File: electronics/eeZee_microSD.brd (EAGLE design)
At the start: 19.8 x 18.3 mm, 13 parts, among them U1 MIC5317, U2 74HC4050, U4 MICROSD_CD

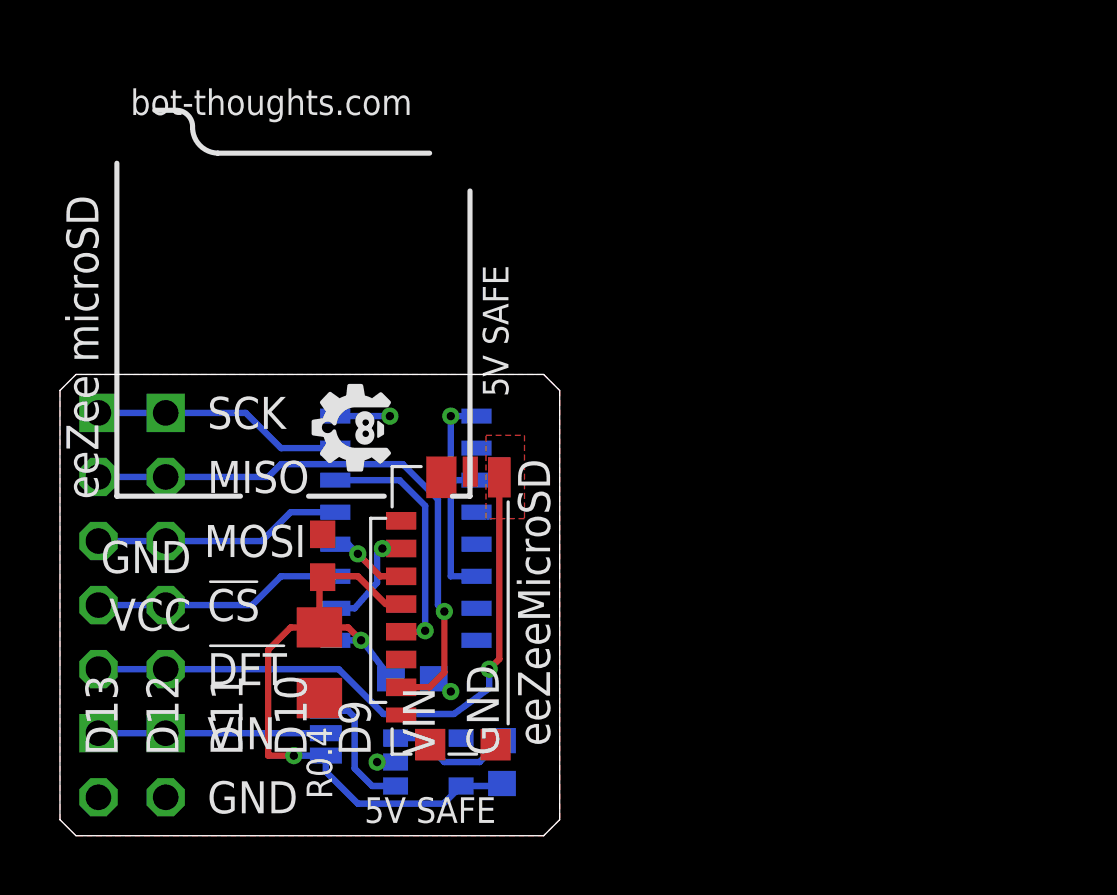
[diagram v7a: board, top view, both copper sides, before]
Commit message: convert to single component layer
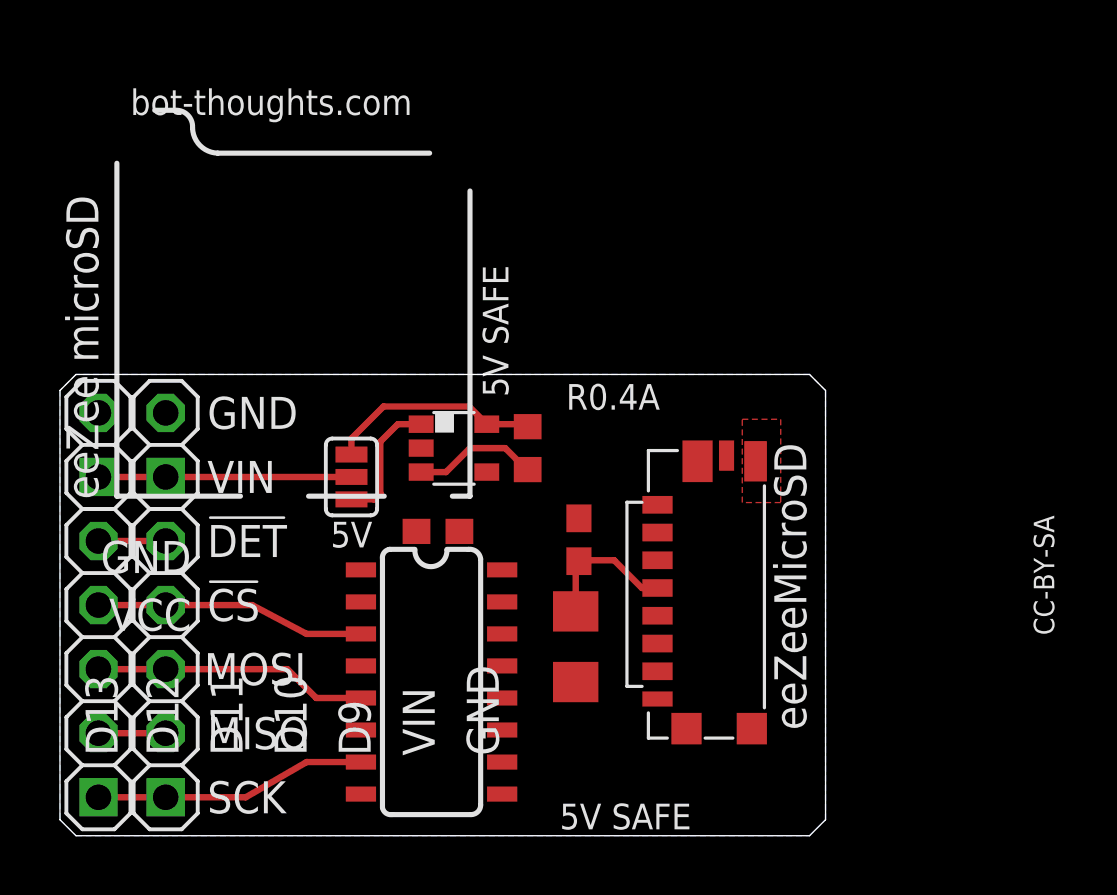
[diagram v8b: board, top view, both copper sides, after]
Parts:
- moved U$5 22.5 mm to (34.7, 9.53), flipped to the bottom
- moved JP1 12.7 mm to (4.19, 15.5), flipped to the top, turned to 90 degrees
- moved JP2 12.7 mm to (1.52, 15.5), flipped to the top, turned to 90 degrees
- moved R5 12.5 mm to (18.5, 15.4), flipped to the top, turned to 270 degrees
- moved U1 12.5 mm to (15.6, 15.4), flipped to the top, turned to 270 degrees
- moved 5V 10.2 mm to (11.6, 14.2), flipped to the top, turned to 270 degrees
- moved C3 10.2 mm to (20.6, 11.7)
- moved C1 10.2 mm to (20.4, 7.49)
- moved U4 10.2 mm to (22.5, 9.27)
- moved U2 6.18 mm to (14.7, 6.10), flipped to the top, turned to 270 degrees
- moved C2 5.93 mm to (15.0, 12.1), flipped to the top, turned to 0 degrees
- moved JP3 5.08 mm to (1.52, 6.60), flipped to the top, turned to 90 degrees
- moved JP4 5.08 mm to (4.19, 6.60), flipped to the top, turned to 90 degrees
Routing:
- net CD: track 25.1 -> 2.67 mm, vias 1 -> 0
- net MISO: track 23.2 -> 2.67 mm, vias 1 -> 0
- net VCC: track 27.8 -> 14.1 mm, vias 2 -> 0
- net GND: track 13.3 -> 0.00 mm, vias 4 -> 0
- net SCK: track 9.90 -> 0.00 mm, vias 1 -> 0
- net !SS: track 4.30 -> 0.00 mm, vias 1 -> 0
- net MOSI: track 3.14 -> 0.00 mm, vias 1 -> 0
- net VIN: track 9.02 -> 10.0 mm
- net MOSI_HV: track 9.87 -> 10.9 mm
- net !CS_HV: track 9.87 -> 10.7 mm
- net SCK_HV: track 9.97 -> 10.8 mm
- added copper zone on layer 16, net GND
- removed copper zone on layer 1, net GND
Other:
- board size 19.8 x 18.3 mm -> 30.4 x 18.3 mm
- board text added: "R0.4A"
- board text removed: "R0.4"
- board text removed: "VIN="
